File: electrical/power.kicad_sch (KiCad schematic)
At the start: 78 parts, among them J1 Conn_01x01_Pin, J2 Conn_01x01_Socket, J3 Conn_01x01_Socket, J4 Conn_01x01_Pin, J5 Conn_01x01_Pin, J6 Conn_01x01_Socket

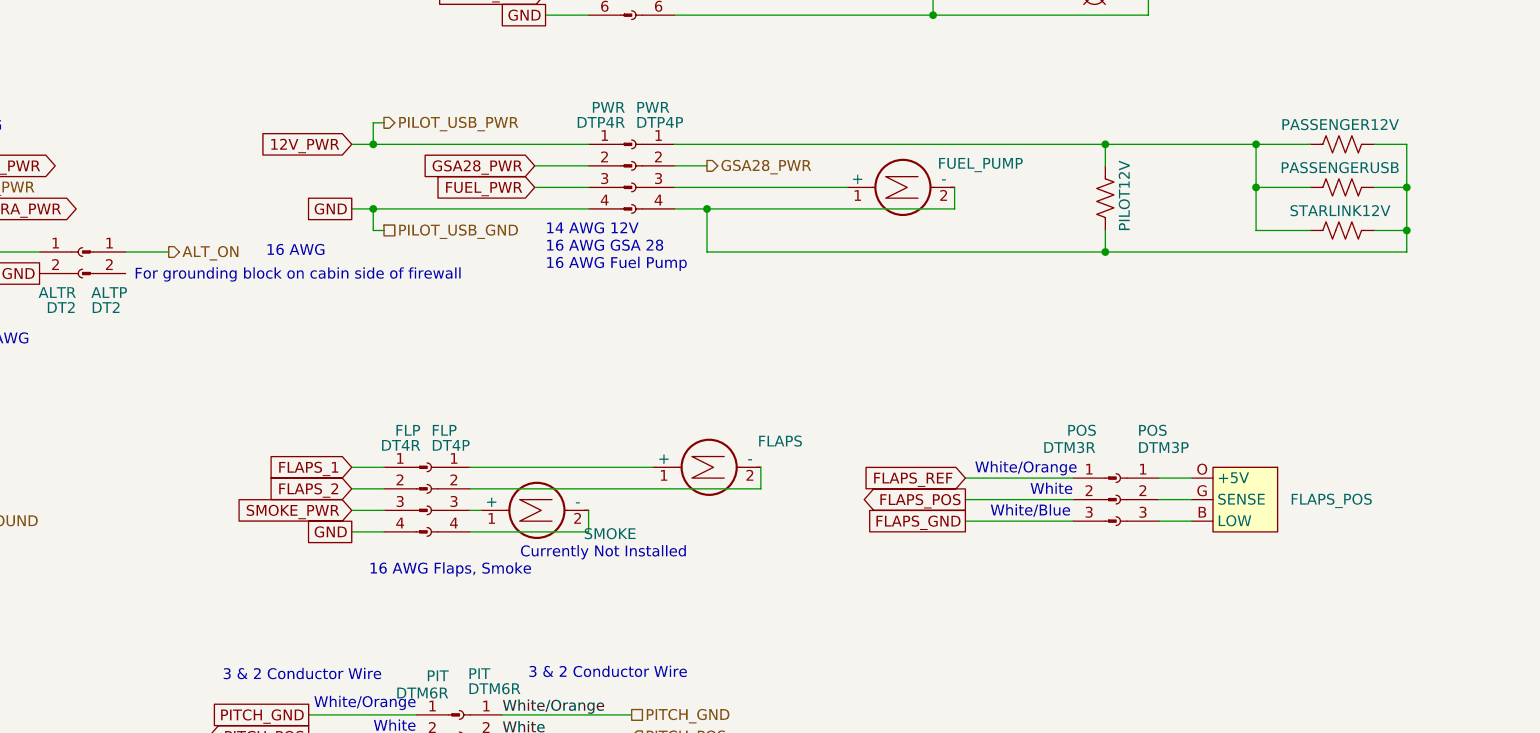
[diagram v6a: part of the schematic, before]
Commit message: Added Flaps Wire Colors. Added Fuel Pump Wire Colors.
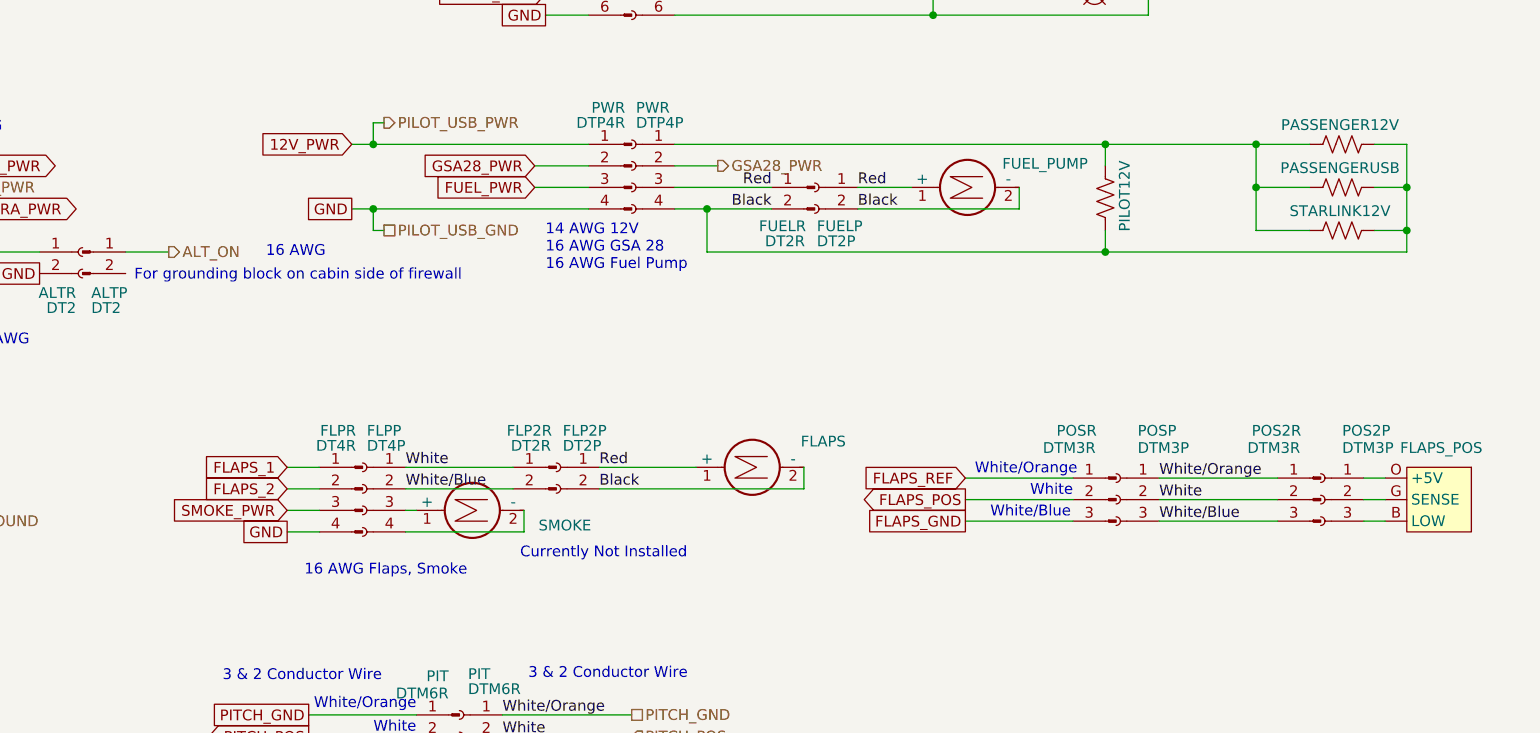
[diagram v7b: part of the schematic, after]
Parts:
- added FLP2P, FUELP: DT2P, symbol Connector:Conn_01x02_Socket
- added FLP2R, FUELR: DT2R, symbol Connector:Conn_01x02_Pin
- added POS2P: DTM3P, symbol Connector:Conn_01x03_Socket
- added POS2R: DTM3R, symbol Connector:Conn_01x03_Pin
- renumbered FLP to FLPP, FLP to FLPR, POS to POSP, POS to POSR
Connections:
- net Black: now also FLAPS.2 (-), FUEL_PUMP.2 (-), PASSENGER12V.1, PASSENGERUSB.1, PILOT12V.1, PWR.4 (Pin_4), STARLINK12V.1, FLP2P.2 (Pin_2), FUELP.2 (Pin_2), FUELR.2 (Pin_2)
- net FLAPS_GND: now also FLPP.2 (Pin_2), POSP.3 (Pin_3), FLP2R.2 (Pin_2), POS2R.3 (Pin_3)
- net FLAPS_POS: now also FLPP.1 (Pin_1), POSP.2 (Pin_2), FLP2R.1 (Pin_1), POS2R.2 (Pin_2)
- net FLAPS_REF: now also POSP.1 (Pin_1), POS2R.1 (Pin_1)
- net Red: now also FLAPS.1 (+), FUEL_PUMP.1 (+), PWR.3 (Pin_3), FLP2P.1 (Pin_1), FUELP.1 (Pin_1), FUELR.1 (Pin_1)
- net at FLAPS_POS.O (+5V): now also POS2P.1 (Pin_1); no longer POSP.1 (Pin_1)
- net at FLAPS_POS.G (SENSE): now also POS2P.2 (Pin_2); no longer POSP.2 (Pin_2)
- net at FLAPS_POS.B (LOW): now also POS2P.3 (Pin_3); no longer POSP.3 (Pin_3)
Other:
- moved on the sheet: FLAPS, FLAPS_POS, FLPP, FLPR, FUEL_PUMP, SMOKE
